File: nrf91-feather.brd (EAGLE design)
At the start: 50.8 x 22.9 mm, 61 parts, among them J1 CON-USB-1050170001, J2 CON-HEADER-1X12-MALE-PIN, J3 CON-HEADER-1X16-MALE-PIN, J4 1909763-1, J5 104224-0820, J6 CON-S2B-PH-SM4-TB(LF)(SN), J9 CON-0002, Q1 MOSFET-P-SC89, Q2 MOSFET-DUAL-COMP-VMT6, Q3 MOSFET-P-30V-4.3A-SOT23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

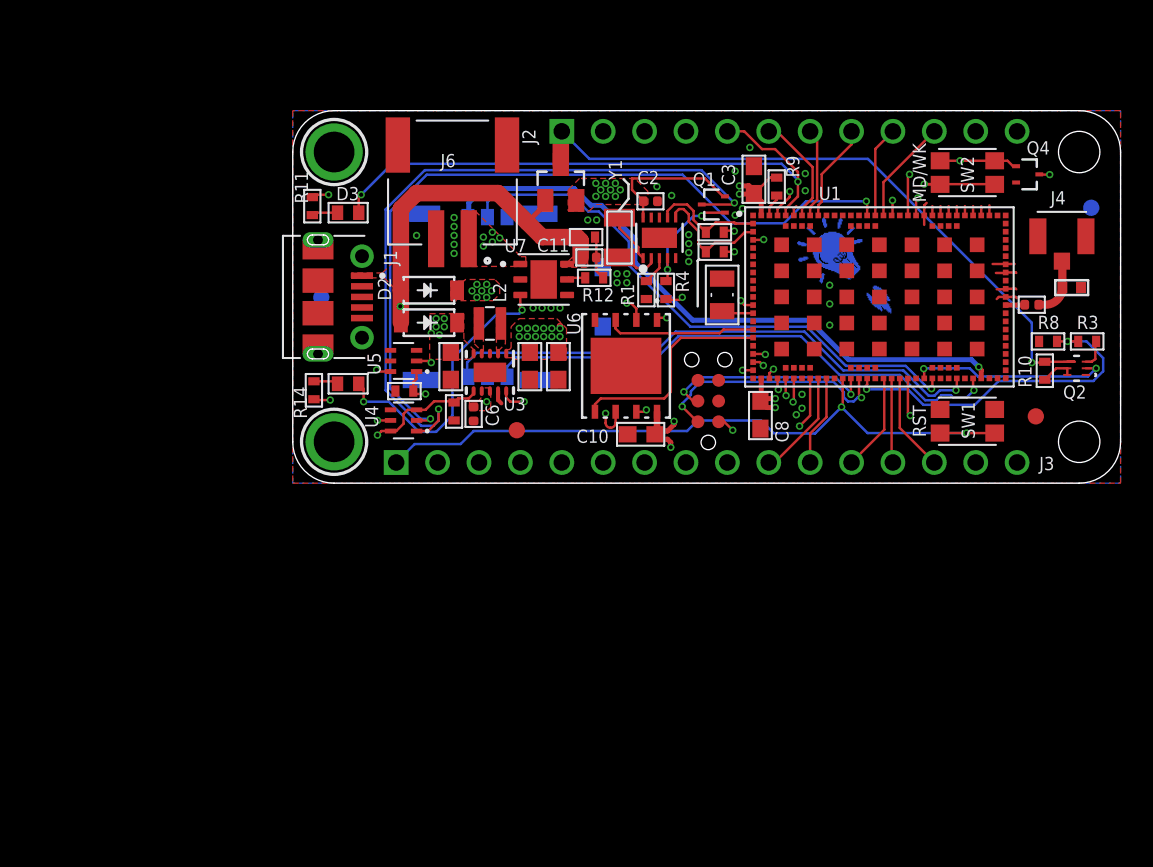
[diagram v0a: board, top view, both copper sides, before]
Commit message: Adding parallel LDO for low power op. (without need to shut everything off)
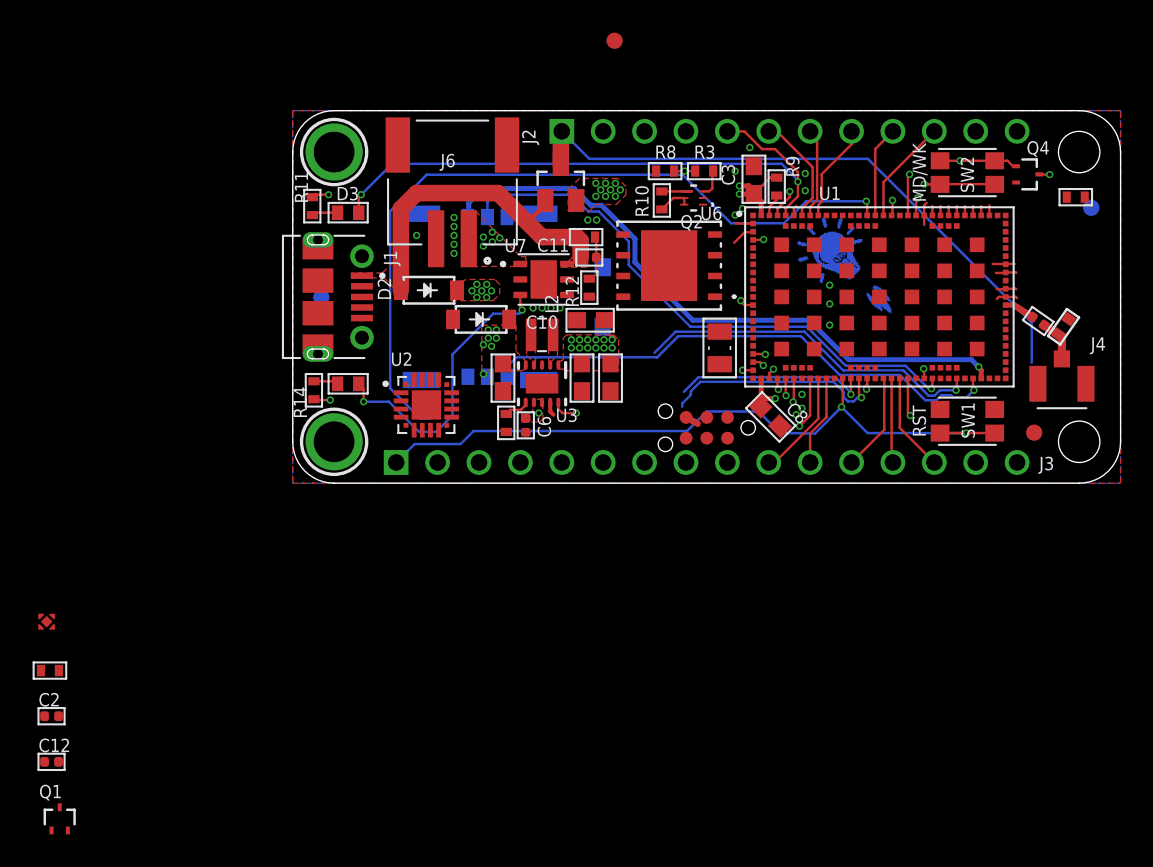
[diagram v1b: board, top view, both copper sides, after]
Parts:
- removed R4: 100k, wolff-den:R0402-M
- removed R5, R6: 20k, wolff-den:R0402-M
- removed U5: IC-BAV70S, wolff-den:SOT363
- removed Y1: XTAL-ABS07AIG-32.768KHZ-7-T, wolff-den:XTAL320X150X90
- added C12: 1u, wolff-den:CAPC1005X55N
- C2: value 0.1u -> 1u
- Q1: value MOSFET-P-SC89 -> MOSFET-N-SC89
- R1: value 100k -> 1M
- U2: value IC-PCF85063ATL/1 -> IC-CP2102N-A02-GQFN20R; device wolff-den:DFN10_2P7X2P7-L -> wolff-den:SILABS_CP2102N-A02-GQFN20R
- U4: value IC-BAV70S -> (none); device wolff-den:SOT363 -> wolff-den:DFN4
- moved Q1 55.0 mm to (-14.3, -20.6), turned to 0 degrees
- moved C2 48.5 mm to (-14.8, -14.3)
- moved R1 43.4 mm to (-14.9, -11.5), turned to 0 degrees
- moved R13 42.9 mm to (48.0, 17.6)
- moved Q2 25.7 mm to (24.6, 17.5)
- moved R10 25.7 mm to (22.6, 17.4)
- moved R3 25.7 mm to (25.2, 19.1)
- moved R8 25.7 mm to (22.9, 19.1)
- moved U4 25.1 mm to (-15.1, -8.50), turned to 0 degrees
- moved U$34 24.6 mm to (19.8, 27.1)
- moved U2 17.6 mm to (8.20, 4.80), turned to 0 degrees
- moved J4 9.05 mm to (47.2, 6.10), turned to 180 degrees
- moved C10 7.66 mm to (18.3, 10.0)
- moved U6 6.70 mm to (23.1, 13.3), turned to 180 degrees
- moved C6 3.28 mm to (14.3, 3.55)
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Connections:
- removed net 3V3_EN: R2.2, U3.6, U4.3, U4.6, U5.6
- removed net N$10: U2.1, Y1.2
- removed net N$18: U2.2, Y1.1
- removed net P0.05/RTC_SCL: R6.1, U1.2, U2.7
- removed net P0.06/RTC_SDA: R5.1, U1.3, U2.6
- removed net RTC_INT: Q1.1, R4.1, U2.4
- removed net RTC_PS_EN: Q1.3, U4.1
- new net D+: J1.3, U2.4
- new net D-: J1.2, U2.5
- new net P0.05/USB_UART_RX: U1.2, U2.18
- new net P0.06/USB_UART_TX: U1.3, U2.17
- new net VREGIN: U2.7
- net +3V3: now also C2.1, U2.6, U4.1; no longer R5.2, R6.2
- net EN: now also R1.1, U4.3; no longer U5.2
- net GND: now also C12.2, U2.12, U2.21, U2.3, U4.2; no longer R1.1, U2.11, U2.5
- net MODE: no longer U5.1
- net N$9: now also Q1.2, R12.2; no longer R1.2, U2.3
- net P0.31/NRF_PS_EN: now also R2.2, U3.6; no longer U4.2
- net PROG: now also Q1.3; no longer R12.2
- net VBUS: now also Q1.1, U2.8; no longer U4.5
- net VSYS: now also C12.1, R1.2, U4.4; no longer C2.1, Q1.2, R4.2, U2.10
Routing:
- net RTC_PS_EN: track 43.7 -> 0.00 mm, vias 2 -> 0
- net VSYS: track 65.5 -> 45.3 mm, vias 18 -> 17
- net P0.20/VBAT_MEAS: track 21.3 -> 2.08 mm
- net P0.12/MD: track 44.0 -> 25.5 mm
- net MODE: track 48.1 -> 29.9 mm, vias 2 -> 1
- net FLASH_SI: track 13.4 -> 0.01 mm
- net FLASH_SCK: track 14.0 -> 0.73 mm, vias 2 -> 1
- net 3V3_EN: track 13.1 -> 0.00 mm, vias 2 -> 0
- net SIM_CLK: track 34.2 -> 21.7 mm
- net P0.25/VBAT_MEAS_EN: track 12.3 -> 0.66 mm, vias 2 -> 1
- net FLASH_SO: track 23.6 -> 12.6 mm, vias 2 -> 1
- net FLASH_HOLD: track 10.3 -> 0.76 mm, vias 2 -> 1
- net FLASH_WP: track 9.19 -> 0.00 mm
- net P0.06/RTC_SDA: track 7.48 -> 0.00 mm
- net EN: track 21.6 -> 14.2 mm
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
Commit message: Current tweaks
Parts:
- added C13, C15: 4.7u, wolff-den:C0603
- added C14, C16: 0.1u, wolff-den:CAPC1005X55N
- added D5: DIO-TVS-DUAL-CA-1, wolff-den:SOT23
- added Q5, Q6: MOSFET-N-SC89, wolff-den:DIO_RB558WMF-L
- added R15, R16, R5, R6: 100k, wolff-den:R0402-M
- added R4: 1k, wolff-den:R0402-M
- moved C12 50.4 mm to (22.4, 16.9)
- moved C2 50.2 mm to (22.2, 19.7), turned to 180 degrees
- moved U4 46.1 mm to (22.4, 18.3), turned to 270 degrees
- moved R1 46.1 mm to (20.9, 17.5), turned to 270 degrees
- moved Q1 44.0 mm to (17.3, 10.0), turned to 180 degrees
- moved U$34 27.1 mm to (5.85, 3.85)
- moved J9 15.3 mm to (12.7, 3.80), turned to 0 degrees
- moved U2 12.7 mm to (20.7, 7.20), turned to 90 degrees
- moved R13 3.92 mm to (45.0, 19.9), turned to 180 degrees
- moved R2 3.85 mm to (9.30, 3.10), turned to 0 degrees
- moved C6 3.38 mm to (11.1, 4.65)
- moved U3 3.38 mm to (12.1, 7.20)
- moved C7 3.38 mm to (9.70, 7.60)
- moved L2 3.38 mm to (12.1, 10.2)
- moved R12 3.36 mm to (15.1, 10.7), turned to 0 degrees
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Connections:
- removed net D+: J1.3, U2.4
- removed net D-: J1.2, U2.5
- removed net EN: J2.2, R1.1, U4.3
- removed net VREGIN: U2.7
- new net !EN: J2.2, Q5.1, Q6.1, R6.1
- new net CP2102N-!RST: R4.1, U2.9
- new net CP2102N-VDD: C15.1, C16.1, U2.6
- new net CRUMPIT_EN: Q6.3, R1.1, U4.3
- new net DIFF_N: D5.2, J1.2, U2.5
- new net DIFF_P: D5.1, J1.3, U2.4
- new net N$10: Q5.3, R5.1, U3.6
- new net N$11: R15.1, R16.2, U2.8
- net +3V3: no longer U2.6
- net GND: now also C13.2, C14.2, C15.2, C16.2, D5.3, Q5.2, Q6.2, R16.1, R6.2
- net P0.31/NRF_PS_EN: now also R5.2; no longer U3.6
- net VBUS: now also C13.1, C14.1, R15.2, R4.2, U2.7; no longer U2.8
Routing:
- net P0.20/VBAT_MEAS: track 2.08 -> 42.7 mm, vias 2 -> 3
- net !EN: track 0.00 -> 37.8 mm, vias 0 -> 1
- net P0.25/VBAT_MEAS_EN: track 0.66 -> 31.5 mm, vias 1 -> 2
- net DIFF_N: track 0.00 -> 29.4 mm, vias 0 -> 2
- net P0.12/MD: track 25.5 -> 53.1 mm
- net VBAT: track 49.2 -> 22.2 mm, vias 5 -> 6
- net DIFF_P: track 0.00 -> 26.1 mm, vias 0 -> 2
- net MODE: track 29.9 -> 5.94 mm, vias 1 -> 0
- net P0.05/USB_UART_RX: track 1.08 -> 18.9 mm, vias 0 -> 2
- net VSYS: track 45.3 -> 61.2 mm
- net VBUS: track 28.3 -> 44.1 mm, vias 0 -> 4
- net P0.06/USB_UART_TX: track 1.44 -> 16.9 mm, vias 0 -> 2
- net FLASH_SCK: track 0.73 -> 15.8 mm, vias 1 -> 2
- net EN: track 14.2 -> 0.00 mm, vias 1 -> 0
- net SIM_CLK: track 21.7 -> 34.8 mm
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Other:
- board text added: "!En"
- board text removed: "En"

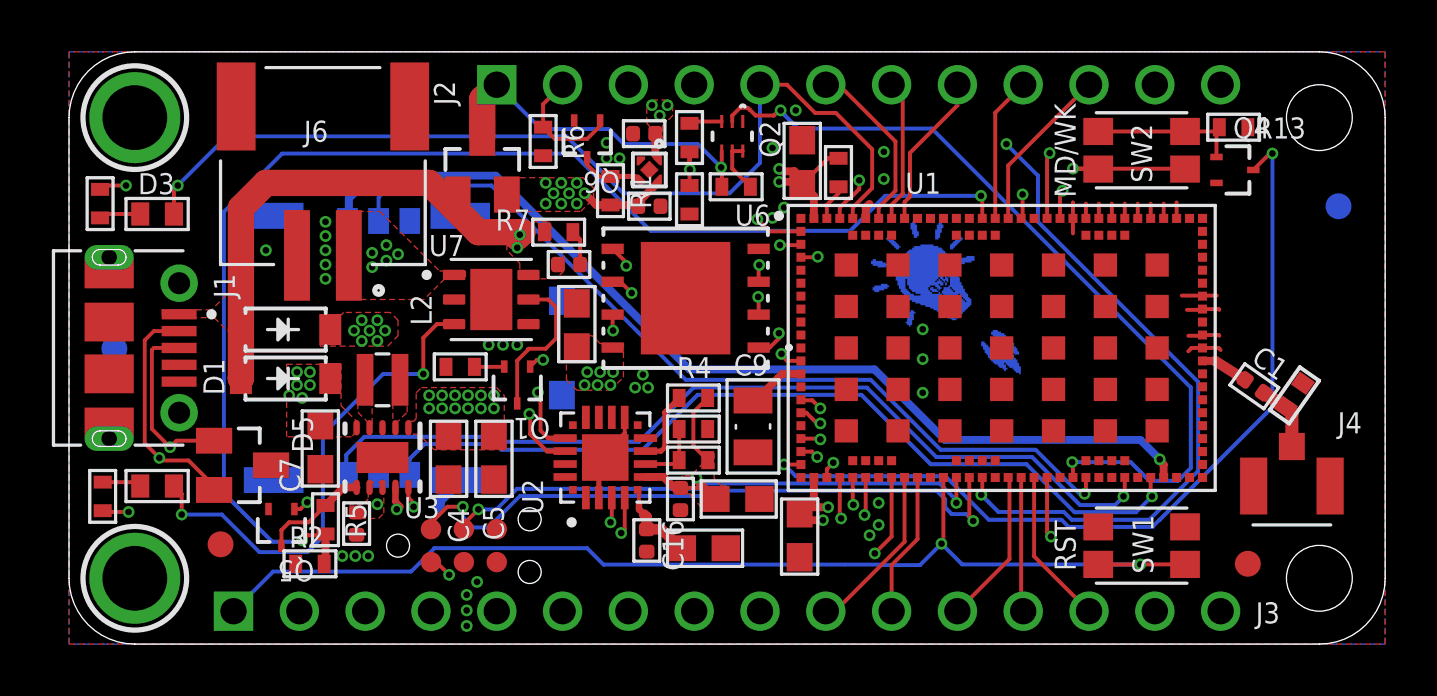
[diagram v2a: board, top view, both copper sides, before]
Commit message: Removing LDO. Cleaning up traces. Fixing slot issue! Adding timer back.
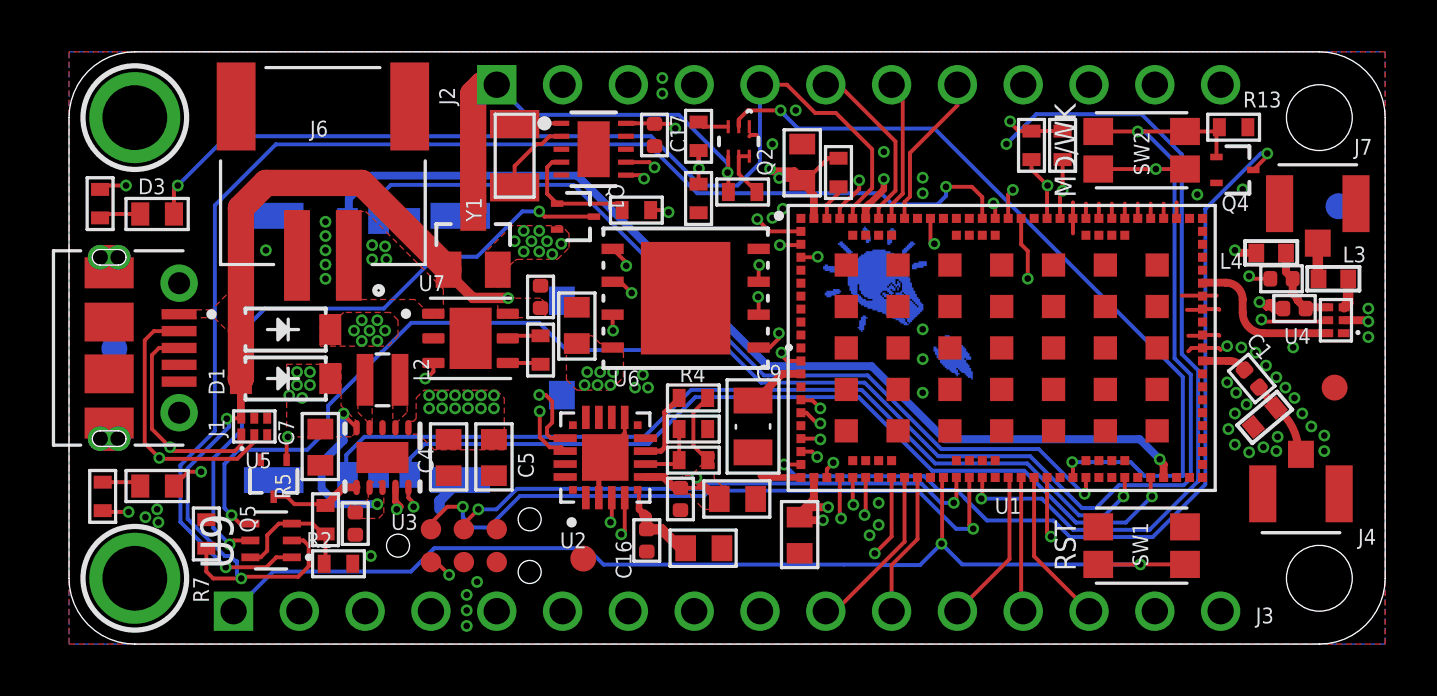
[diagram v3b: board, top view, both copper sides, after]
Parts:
- removed D5: DIO-TVS-DUAL-CA-1, wolff-den:SOT23
- removed Q6: MOSFET-N-SC89, wolff-den:DIO_RB558WMF-L
- removed R1: 1M, wolff-den:R0402-M
- added C17: 0.1u, wolff-den:CAPC1005X55N
- added J7: 1909763-1, wolff-den:TE_1909763-1
- added L3, L4: 3.9n, wolff-den:IND0402_22N_TAI
- added R17, R18: 20k, wolff-den:R0402-M
- added U5: IC-TPD4S012DRYR, wolff-den:PSON50P100X145X50-6N
- added U8: IC-PCF85063ATL/1, wolff-den:DFN10_2P7X2P7-L
- added U9: IC-BAV70S, wolff-den:SOT363
- added Y1: XTAL-ABS07AIG-32.768KHZ-7-T, wolff-den:XTAL320X150X90
- C12: value 1u -> 100p
- C2: value 1u -> 0.1u
- Q1: value MOSFET-N-SC89 -> MOSFET-P-SC89
- U4: value (none) -> BGU6005,115; device wolff-den:DFN4 -> wolff-den:PSON50P100X145X50-6N
- moved U4 27.1 mm to (48.9, 12.5), turned to 180 degrees
- moved C2 25.2 mm to (46.8, 14.1)
- moved C12 25.2 mm to (47.3, 12.9), turned to 180 degrees
- moved R7 17.9 mm to (5.30, 4.25), turned to 270 degrees
- moved U$34 14.0 mm to (19.9, 3.30)
- moved U$35 7.58 mm to (48.9, 9.90)
- moved Q1 6.88 mm to (19.6, 16.5), turned to 270 degrees
- moved R6 4.47 mm to (21.9, 16.8), turned to 0 degrees
- moved R12 3.17 mm to (18.2, 11.3), turned to 90 degrees
- moved Q3 2.92 mm to (15.6, 15.6)
- moved Q5 1.92 mm to (7.90, 6.40)
- moved U$1 1.86 mm to (35.2, 10.1)
- moved U7 1.70 mm to (15.5, 11.8)
- moved C11 1.67 mm to (18.2, 13.4), turned to 90 degrees
- moved L1 1.43 mm to (46.1, 8.75), turned to 40 degrees
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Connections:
- net N$10 renamed PS_EN
- net N$3 renamed ANT
- removed net CRUMPIT_EN: Q6.3, R1.1, U4.3
- removed net N$9: Q1.2, R12.2
- new net GPS: U1.67, U4.6
- new net GPS_AMP: L3.2, U4.3
- new net GPS_CON: J7.1, L3.1
- new net LNA_EN: U1.93, U4.5
- new net N$10: U8.1, Y1.2
- new net N$18: U8.2, Y1.1
- new net PS_EN_CC: R2.2, R5.2, U9.3, U9.6
- new net RTC_INT: Q1.1, R6.1, U8.4
- new net RTC_PS_EN: Q1.3, U9.5
- new net VCC_LNA_FILT: C12.1, C2.1, L4.2, U4.4
- net !EN: no longer Q6.1, R6.1
- net +3V3: now also L4.1, R17.2, R18.2; no longer C2.1, U4.1
- net DIFF_N: now also U5.2; no longer D5.2
- net DIFF_P: now also U5.1; no longer D5.1
- net GND: now also C17.2, J1.SH10, J1.SH9, J7.2, J7.3, U4.1, U5.4, U8.11, U8.3, U8.5; no longer D5.3, Q6.2, R6.2
- net MODE: now also U9.4
- net P0.26/SDA: now also R17.1, U8.6
- net P0.27/SCL: now also R18.1, U8.7
- net P0.31/NRF_PS_EN: now also U9.1; no longer R2.2, R5.2
- net PROG: now also R12.2; no longer Q1.3
- net VBUS: now also U5.6, U9.2; no longer Q1.1
- net VSYS: now also C17.1, Q1.2, R6.2, U8.10; no longer C12.1, R1.2, U4.4
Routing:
- net MODE: track 5.94 -> 66.8 mm, vias 0 -> 2
- net RTC_PS_EN: track 0.00 -> 25.4 mm, vias 0 -> 2
- net P0.27/SCL: track 7.71 -> 28.6 mm, vias 1 -> 2
- net P0.26/SDA: track 8.96 -> 28.3 mm, vias 1 -> 2
- net !EN: track 37.8 -> 19.8 mm
- net LNA_EN: track 0.00 -> 17.6 mm, vias 0 -> 2
- net VBUS: track 44.1 -> 55.9 mm
- net GND: track 19.2 -> 28.4 mm, vias 35 -> 63
- net CHRG: track 19.1 -> 12.2 mm
- net GPS: track 0.00 -> 5.94 mm
- net PS_EN_CC: track 0.00 -> 5.36 mm
- net P0.20/VBAT_MEAS: track 42.7 -> 47.7 mm
- net RTC_INT: track 0.00 -> 4.81 mm
- net PROG: track 5.91 -> 1.31 mm
- net VCC_LNA_FILT: track 0.00 -> 3.34 mm
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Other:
- board text removed: "TODO: 1. Antenna stuff"

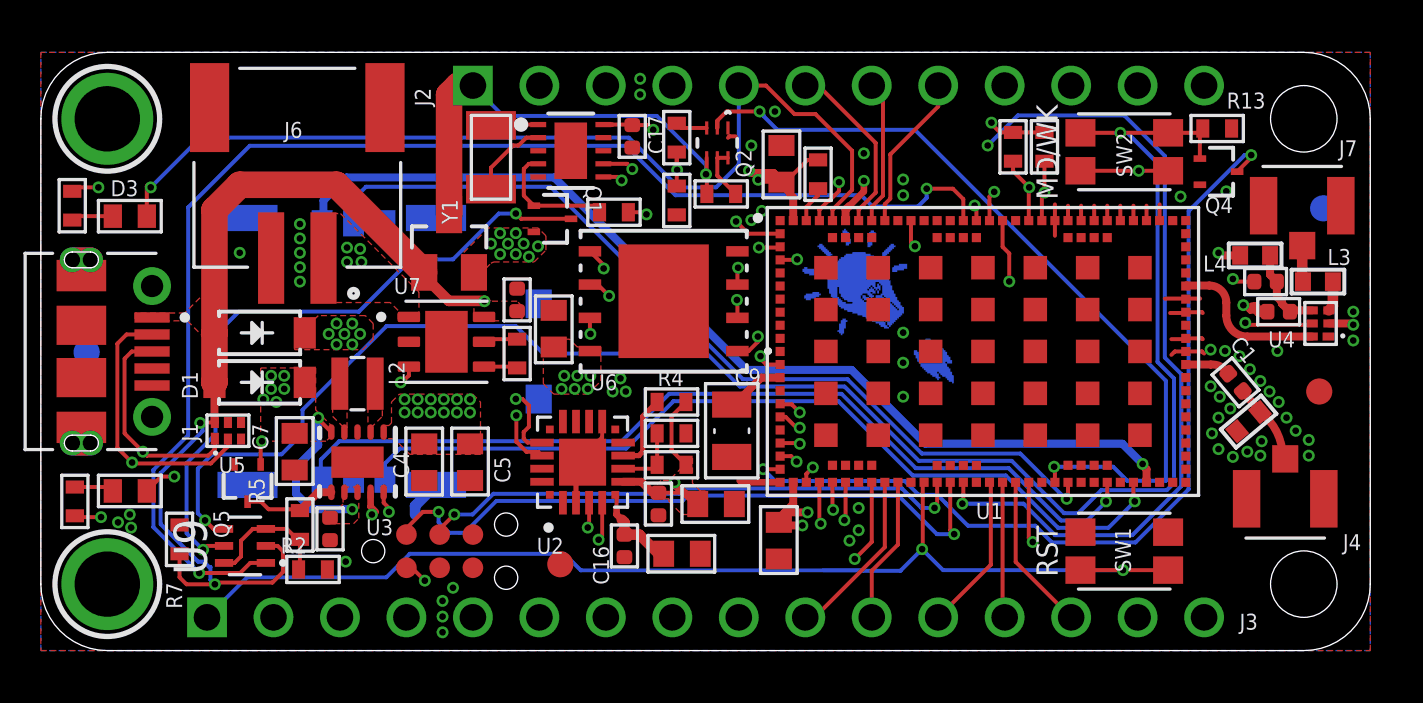
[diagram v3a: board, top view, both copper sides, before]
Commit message: 1. Add doc outline 2. Adding tdocu 3. Exporting assembly docs using cam2print PDF 4. Updating nRF91 footprint
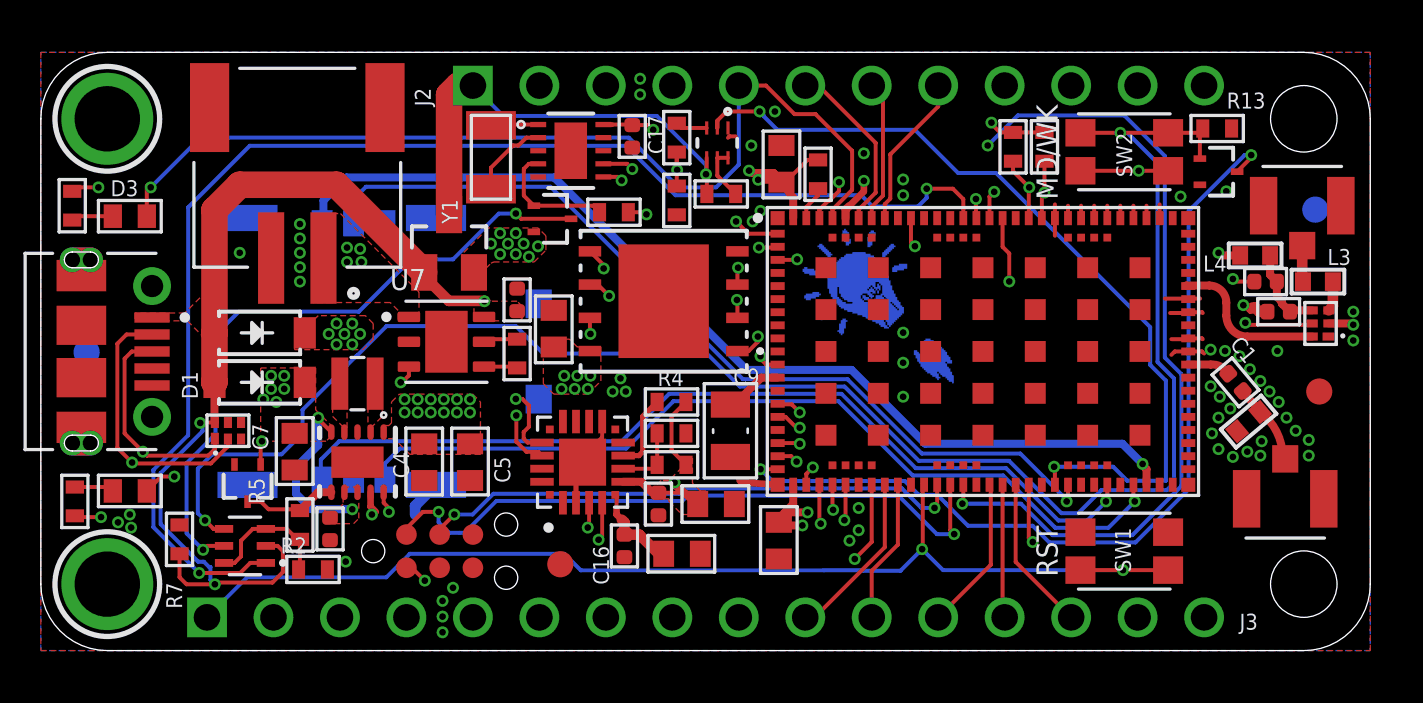
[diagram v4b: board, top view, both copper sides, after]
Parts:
- added U$5: (no value), frames:A3L-LOC
- moved U$3 0.30 mm to (48.7, 16.9)
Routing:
- net P0.25/VBAT_MEAS_EN: track 31.0 -> 32.0 mm
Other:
- board text added: "(Top down)"
- board text added: "BOT"
- board text added: "Confidential - Property of Circuit Dojo LLC"
- board text added: "Notes: * T4 solder paste * Lead Free assembly * Measures in mm"
- board text added: "TOP"
- board text added: "nRF9160 Featherwing"

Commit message: 1. Clean  up silk 2. Updated 3D packages 3. Pushed to OSH Park + Fusion 4. Added 1.8V LDO for LNA
Proto2
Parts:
- added C18, C19: 1u, wolff-den:CAPC1005X55N
- added R1: 100k, wolff-den:R0402-M
- added U10: (no value), wolff-den:DFN4
- L3, L4: value 3.9n -> 5.6n
- R15: value 100k -> 22.1k
- R16: value 100k -> 47.5k
- moved U$5 240.1 mm to (26.1, 26.6), turned to 90 degrees
- moved U$35 7.54 mm to (45.3, 3.25)
- moved C9 0.27 mm to (26.4, 8.65)
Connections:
- new net VCC_1V8: C19.1, L4.1, U10.1
- net +3V3: now also C18.1, U10.4; no longer L4.1
- net GND: now also C18.2, C19.2, R1.1, U10.2
- net LNA_EN: now also R1.2, U10.3; no longer U4.5
- net VCC_LNA_FILT: now also U4.5
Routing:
- net VCC_1V8: track 0.00 -> 9.17 mm, vias 0 -> 2
- net LNA_EN: track 17.7 -> 25.2 mm
- net GND: track 28.2 -> 34.6 mm, vias 63 -> 64
- net +3V3: track 17.3 -> 18.4 mm
- net VCC_LNA_FILT: track 3.34 -> 3.84 mm
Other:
- board text removed: "MD/WK"
